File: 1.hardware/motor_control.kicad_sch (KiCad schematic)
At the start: 0 parts

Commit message: 중간 저장
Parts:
- added C17: 4.7uF/10V, symbol Device:C_Small_US
- added J10: MOTOR_UVW, symbol Connector_Generic:Conn_01x03
- added J11: HALL_SENSOR, symbol Connector_Generic:Conn_01x05
- added R1, R97, R98: 0.2R, symbol Device:R_Shunt_US
- added U7, U8: LM2904D, PCM_Package_SO_AKL:SO-8_3.9x4.9mm_P1.27mm, symbol PCM_Amplifier_Operational_AKL:LM2904D
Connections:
- new net 5V: C17.1, J11.1 (Pin_1)
- new net GND: C17.2, J11.2 (Pin_2)
- new net HALL_A: J11.3 (Pin_3)
- new net HALL_B: J11.4 (Pin_4)
- new net HALL_C: J11.5 (Pin_5)
- new net MOTOR_U: J10.1 (Pin_1)
- new net MOTOR_V: J10.2 (Pin_2)
- new net MOTOR_W: J10.3 (Pin_3)

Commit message: 중간 수정
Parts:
- added Q10, Q11, Q12, Q13, Q8, Q9: IRFZ44NSTRLPBF, SamacSys_Parts:IRFZ44NSTRLPBF, symbol SamacSys_Parts:IRFZ44NSTRLPBF
- added R125, R126, R129, R130, R132, R133: 10k/0.063w, symbol Device:R_Small_US
- added R127, R128, R131, R134, R135, R2, R3: 10k/0.125w, symbol Device:R_Small_US
- added U12, U13, U14: IR2101, symbol Driver_FET:IR2101
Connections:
- net GND: now also U7.4 (V-), U8.4 (V-)
- net at R98.1: now also Q13.3
- net at R98.2: now also R132.1
- net at R98.3: now also R133.1
- net GNDPWR: now reaches R98.4
- net GNDPWR: now also R1.4, R97.4, U13.4 (COM), U14.4 (COM)
- net CURRENT_W: now reaches U8.1
- net CURRENT_W: now also R131.2
- net at U8.2 (-): now also R131.1, R132.2
- net at U8.3 (+): now also R133.2
- net +3.3V: now reaches U8.8 (V+)
- net +3.3V: now also U7.8 (V+)
- net at R97.1: now also Q9.3
- net at R97.2: now also R126.1
- net at R97.3: now also R125.1
- net CURRENT_U: now reaches U7.1
- net CURRENT_U: now also R127.2
- net at U7.2 (-): now also R126.2, R127.1
- net at U7.3 (+): now also R125.2
- net at U7.5 (+): now also R130.2
- net at U7.6 (-): now also R128.1, R129.2
- net CURRENT_V: now reaches U7.7
- net CURRENT_V: now also R128.2
- net at R1.1: now also Q11.3
- net at R1.2: now also R129.1
- net at R1.3: now also R130.1
- new net: Q9.1, R3.2
- new net: R2.1, U12.7 (HO)
- new net: Q8.1, R2.2
- new net: R3.1, U12.5 (LO)
- no-connect marks 0 -> 3
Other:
- note added: "U_Part"
- note added: "V_Part"
- note added: "W_Part"
- moved on the sheet: C17, J10, J11, R1, R97, R98, U7A, U7B, U8A, U8B

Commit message: 중간 저장
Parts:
- added R136, R137: 10k/0.125w, symbol Device:R_Small_US
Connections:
- net GNDPWR: now also U12.4 (COM)
- net MOTOR_U: now also Q8.3, Q9.2
- net MOTOR_V: now also Q10.3, Q11.2
- net MOTOR_W: now also Q12.3, Q13.2
- net at Q10.1: now also R134.2
- net at U14.5 (LO): now also R137.1
- net at U14.7 (HO): now also R136.1
- net at R135.1: now also U13.5 (LO)
- net at R135.2: now also Q11.1
- net at U13.7 (HO): now also R134.1
- net at Q12.1: now also R136.2
- net at Q13.1: now also R137.2
- no-connect marks 3 -> 0
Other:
- moved on the sheet: C17, J10, J11, Q10, Q11, Q12, Q13, Q8, Q9, R1, R125, R126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

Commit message: 중간저장
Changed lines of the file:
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@@
 	(global_label "MOTOR_U"
 		(shape passive)
-		(at 125.5383 38.7494 180)
+		(at 130.81 38.1 180)
 		(fields_autoplaced yes)
 		(effects
@@
 		)
 		(property "Intersheetrefs" "${INTERSHEET_REFS}"
-			(at 115.0163 38.7494 0)
+			(at 120.288 38.1 0)
 			(effects
 				(font
@@
 	(global_label "MOTOR_V"
 		(shape passive)
-		(at 125.5383 41.2894 180)
+		(at 130.81 40.64 180)
 		(fields_autoplaced yes)
 		(effects
@@
 		)
 		(property "Intersheetrefs" "${INTERSHEET_REFS}"
-			(at 115.2582 41.2894 0)
+			(at 120.5299 40.64 0)
 			(effects
 				(font
@@
 	(global_label "MOTOR_W"
 		(shape passive)
-		(at 125.5383 43.8294 180)
+		(at 130.81 43.18 180)
 		(fields_autoplaced yes)
 		(effects
@@
 		)
 		(property "Intersheetrefs" "${INTERSHEET_REFS}"
-			(at 114.8954 43.8294 0)
+			(at 120.1671 43.18 0)
 			(effects
 				(font

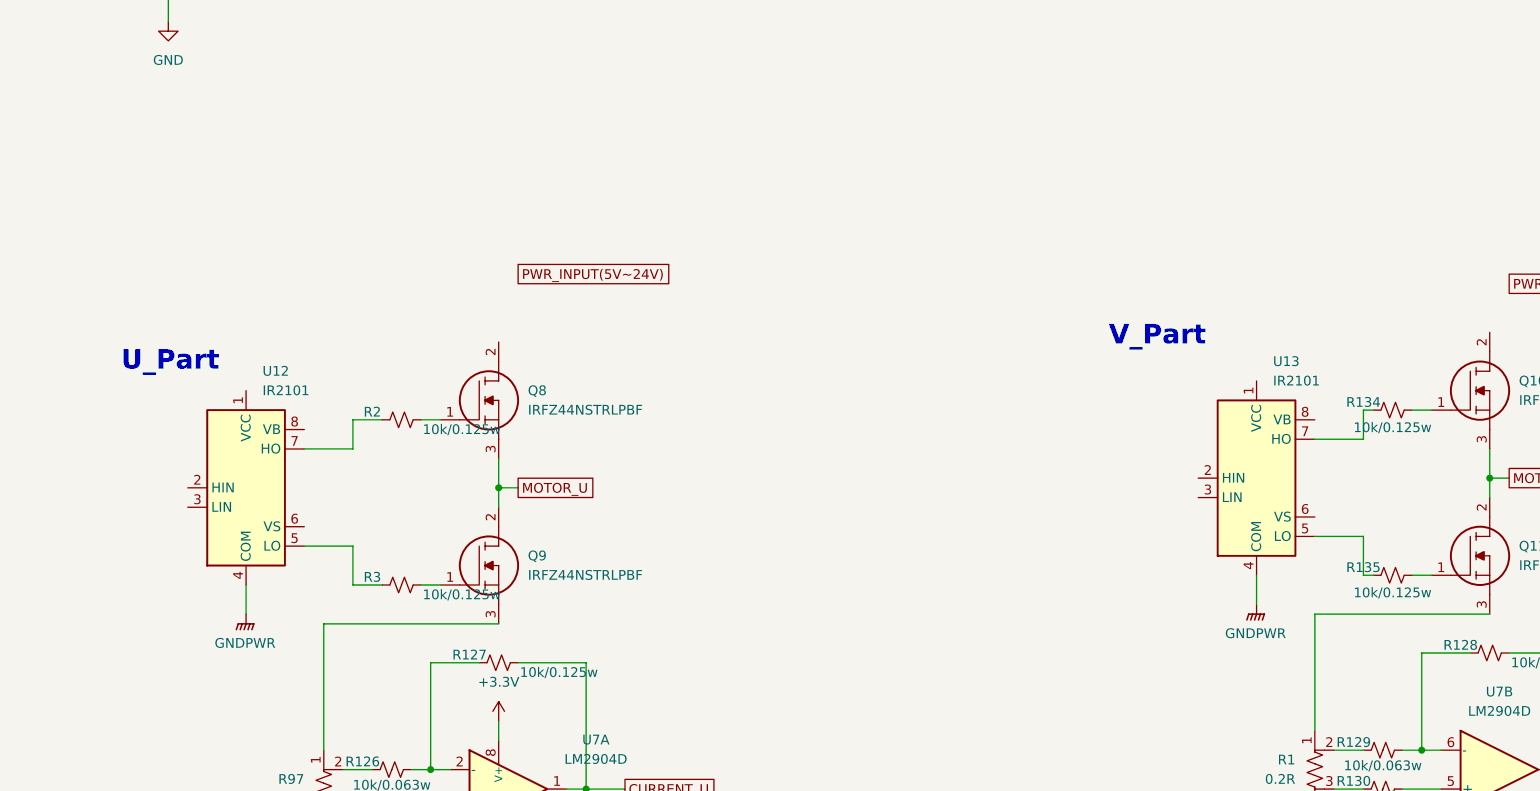
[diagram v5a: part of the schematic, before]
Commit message: 스펙 변경 12~48V 인풋 + 모스펫 구동에 필요한 전압 구현 필요
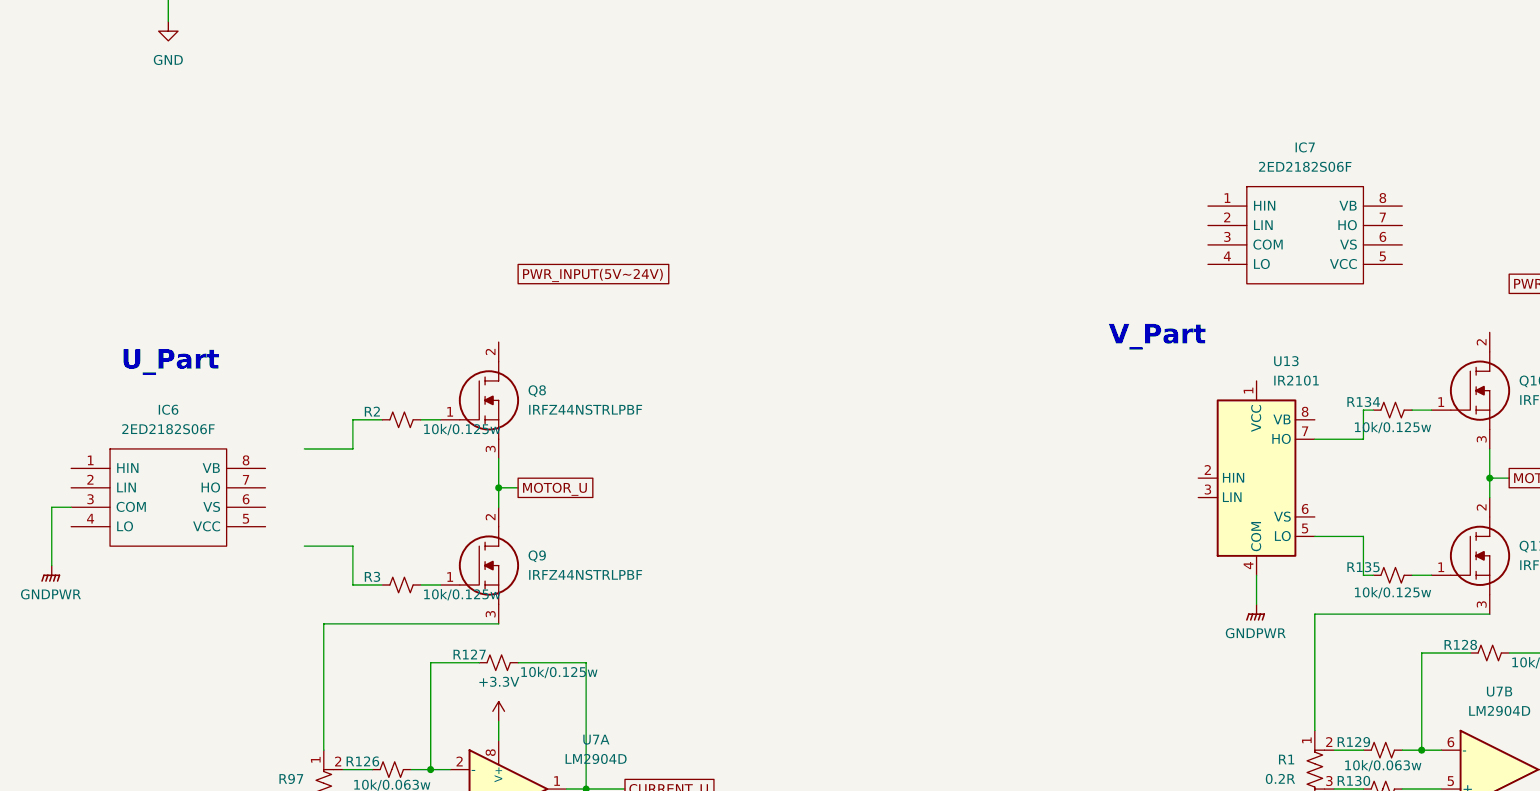
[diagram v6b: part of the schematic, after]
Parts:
- removed U12: IR2101, symbol Driver_FET:IR2101
- added IC6, IC7: 2ED2182S06F, SOIC127P600X172-8N, symbol SamacSys_Parts:2ED2182S06F
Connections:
- net GNDPWR: now also IC6.3 (COM)

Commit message: mosfet 확정 및 드라이버 고려중 자세한 계산식 필요
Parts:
- removed IC6, IC7: 2ED2182S06F, SOIC127P600X172-8N, symbol SamacSys_Parts:2ED2182S06F
- removed Q10, Q11, Q12, Q13, Q8, Q9: IRFZ44NSTRLPBF, SamacSys_Parts:IRFZ44NSTRLPBF, symbol SamacSys_Parts:IRFZ44NSTRLPBF
- added IC1: UCC27712QDRQ1, SOIC127P600X175-8N, symbol SamacSys_Parts:UCC27712QDRQ1
- added IC4: SN74HC266D, SOIC127P600X175-14N, symbol SamacSys_Parts:SN74HC266D
- added Q10, Q2, Q3, Q4, Q8, Q9: STL130N6F7, FERD20U50DJFTR, symbol SamacSys_Parts:STL130N6F7
- J10: value MOTOR_UVW -> MOTOR_1_UVW
- J11: value HALL_SENSOR -> MOTOR_1_HALL_SENSOR

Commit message: 중간 저장
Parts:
- removed IC4: SN74HC266D, SOIC127P600X175-14N, symbol SamacSys_Parts:SN74HC266D
- removed R125, R126, R129, R130, R132, R133: 10k/0.063w, symbol Device:R_Small_US
- removed R127, R128, R131, R134, R135, R136, R137, R2, R3: 10k/0.125w, symbol Device:R_Small_US
- removed U13, U14: IR2101, symbol Driver_FET:IR2101
- removed U7, U8: LM2904D, PCM_Package_SO_AKL:SO-8_3.9x4.9mm_P1.27mm, symbol PCM_Amplifier_Operational_AKL:LM2904D
- added TP13: TP_HA2, symbol Connector:TestPoint
- added TP14: TP_HB2, symbol Connector:TestPoint
- added TP15: TP_HC2, symbol Connector:TestPoint
- added TP16: TP_U2, symbol Connector:TestPoint
- added TP17: TP_V2, symbol Connector:TestPoint
- added TP18: TP_W2, symbol Connector:TestPoint
- R1, R97, R98: value 0.2R -> 0.01R
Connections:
- net MOTOR1_W_SHUNT_P: now reaches R98.2
- net MOTOR1_W_SHUNT_M: now reaches R98.3
- net MOTOR1_U_SHUNT_P: now reaches R97.2
- net MOTOR1_U_SHUNT_M: now reaches R97.3
- net MOTOR1_V_SHUNT_P: now reaches R1.2
- net MOTOR1_V_SHUNT_M: now reaches R1.3
- net HALL_A renamed HALL1_A
- net HALL1_A: now also TP13.1
- net HALL_B renamed HALL1_B
- net HALL1_B: now also TP14.1
- net HALL_C renamed HALL1_C
- net HALL1_C: now also TP15.1
- net MOTOR_U renamed MOTOR1_U
- net MOTOR1_U: now also TP16.1
- net MOTOR_V renamed MOTOR1_V
- net MOTOR1_V: now also TP17.1
- net MOTOR_W renamed MOTOR1_W
- net MOTOR1_W: now also TP18.1
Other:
- moved on the sheet: C17, IC1, J10, J11, Q2, Q3, R98
